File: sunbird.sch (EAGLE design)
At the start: 68 parts, among them J1 USB_MINI-B_SMT, Q8010 600mA/40V, U1000 TP4056, U1500 FS312F-G, U1550 FS8205, U2000 MT3608, U2100 M3406, U4000 FM116B, U5000 CH340G, U6000 RICHTEK-RT3000CGQM, U6001 0.1uF, U6100 HDC1080NOPAD, Y5000 12Mhz

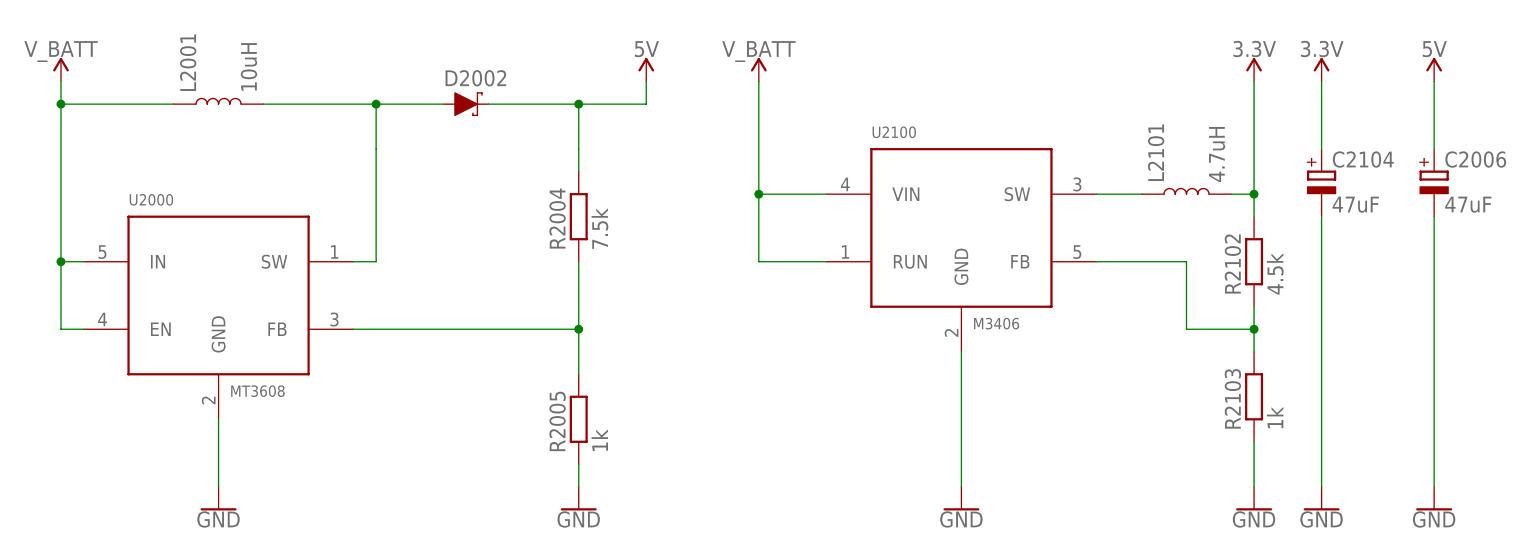
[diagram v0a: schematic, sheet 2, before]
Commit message: Revise PCB to use inductors + 47uF 0603 "miracle" caps from LCSC.
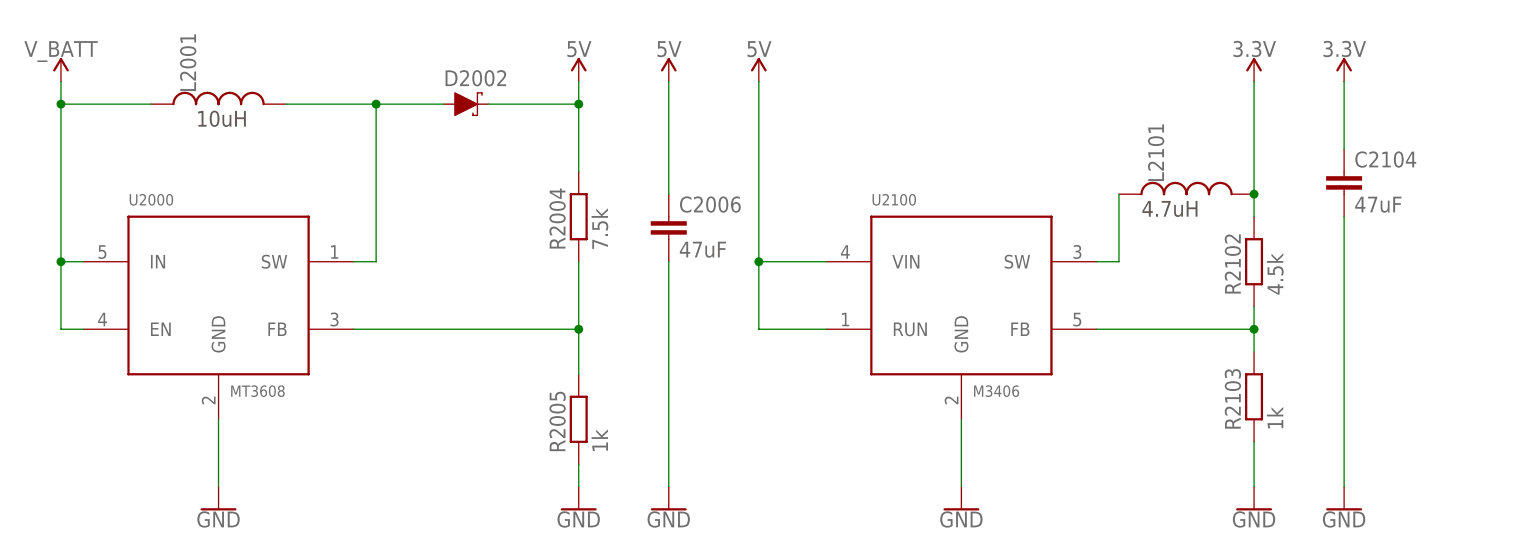
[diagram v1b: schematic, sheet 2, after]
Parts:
- C2006, C2104: device rcl:CPOL-EUUD-5X5,8 -> rcl:C-EUC0603
- L2001, L2101: device SparkFun-Coils:INDUCTOR-0805-3.3UH -> geusebio:INDUCTOR_3.0X3.03.0X3.0
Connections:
- net 3.3V: now also C2104.1; no longer C2104.+
- net 5V: now also C2006.1, U2100.RUN, U2100.VIN; no longer C2006.+
- net GND: now also C2006.2, C2104.2; no longer C2006.-, C2104.-
- net V_BATT: no longer U2100.RUN, U2100.VIN
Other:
- note added: "10uH"
- note added: "4.7uH"
- moved on the sheet: U2100

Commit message: Removing sensor array
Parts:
- removed U6000: RICHTEK-RT3000CGQM, geusebio:RICHTEK-RT3000CGQM
- removed U6001: 0.1uF, rcl:C-EUC0603
- removed U6100: HDC1080NOPAD, geusebio:HDC1080NOPAD
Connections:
- net 3.3V: no longer U6000.VDD, U6000.VDDIO, U6001.1, U6100.VIN
- net ACC_INT/GPIO15: no longer U6000.INT1
- net GND: no longer U6000.GND, U6001.2, U6100.GND
- net SCL/GPIO0: no longer U6000.SCL, U6100.SCL
- net SDA/GPIO4: no longer U6000.SDA, U6100.SDA
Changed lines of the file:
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@@
 <part name="R1009" library="rcl" library_urn="urn:adsk.eagle:library:334" deviceset="R-EU_" device="R0603" package3d_urn="urn:adsk.eagle:package:23555/2" value="2k"/>
 <part name="GND20" library="SparkFun-PowerSymbols" library_urn="urn:adsk.eagle:library:530" deviceset="GND" device=""/>
-<part name="FRAME6" library="SparkFun-Aesthetics" library_urn="urn:adsk.eagle:library:507" deviceset="FRAME-A4L" device=""/>
-<part name="GND21" library="SparkFun-PowerSymbols" library_urn="urn:adsk.eagle:library:530" deviceset="GND" device=""/>
-<part name="SUPPLY23" library="SparkFun-PowerSymbols" library_urn="urn:adsk.eagle:library:530" deviceset="3.3V" device=""/>
-<part name="SUPPLY24" library="SparkFun-PowerSymbols" library_urn="urn:adsk.eagle:library:530" deviceset="3.3V" device=""/>
-<part name="GND22" library="SparkFun-PowerSymbols" library_urn="urn:adsk.eagle:library:530" deviceset="GND" device=""/>
-<part name="U6001" library="rcl" library_urn="urn:adsk.eagle:library:334" deviceset="C-EU" device="C0603" package3d_urn="urn:adsk.eagle:package:23616/2" value="0.1uF"/>
 <part name="R8004" library="rcl" library_urn="urn:adsk.eagle:library:334" deviceset="R-EU_" device="R0603" package3d_urn="urn:adsk.eagle:package:23555/2" value="10k"/>
 <part name="SUPPLY25" library="SparkFun-PowerSymbols" library_urn="urn:adsk.eagle:library:530" deviceset="5V" device=""/>
@@
 <part name="SUPPLY18" library="SparkFun-PowerSymbols" library_urn="urn:adsk.eagle:library:530" deviceset="5V" device=""/>
 <part name="SUPPLY19" library="SparkFun-PowerSymbols" library_urn="urn:adsk.eagle:library:530" deviceset="5V" device=""/>
-<part name="U6000" library="geusebio" deviceset="RICHTEK-RT3000CGQM" device=""/>
 <part name="SUPPLY26" library="SparkFun-PowerSymbols" library_urn="urn:adsk.eagle:library:530" deviceset="5V" device=""/>
-<part name="U6100" library="geusebio" deviceset="HDC1080" device="NOPAD"/>
-<part name="SUPPLY27" library="SparkFun-PowerSymbols" library_urn="urn:adsk.eagle:library:530" deviceset="3.3V" device=""/>
-<part name="GND25" library="SparkFun-PowerSymbols" library_urn="urn:adsk.eagle:library:530" deviceset="GND" device=""/>
 <part name="SUPPLY8" library="SparkFun-PowerSymbols" library_urn="urn:adsk.eagle:library:530" deviceset="5V" device=""/>
 </parts>
@@
 </segment>
 </net>
-</nets>
-</sheet>
-<sheet>
-<description>Sensor Array</description>
-<plain>
-</plain>
-<instances>
-<instance part="FRAME6" gate="G$1" x="0" y="0" smashed="yes">
-<attribute name="DRAWING_NAME" x="181.61" y="11.43" size="2.54" layer="94" font="vector"/>
-<attribute name="LAST_DATE_TIME" x="181.61" y="6.35" size="2.286" layer="94" font="vector"/>
-<attribute name="SHEET" x="195.58" y="1.27" size="2.54" layer="94" font="vector"/>
-</instance>
-<instance part="GND21" gate="1" x="68.58" y="25.4" smashed="yes">
-<attribute name="VALUE" x="68.58" y="25.146" size="1.778" layer="96" align="top-center"/>
-</instance>
-<instance part="SUPPLY23" gate="G$1" x="68.58" y="58.42" smashed="yes">
-<attribute name="VALUE" x="68.58" y="61.214" size="1.778" layer="96" align="bottom-center"/>
-</instance>
-<instance part="SUPPLY24" gate="G$1" x="91.44" y="58.42" smashed="yes">
-<attribute name="VALUE" x="91.44" y="61.214" size="1.778" layer="96" align="bottom-center"/>
-</instance>
-<instance part="GND22" gate="1" x="91.44" y="25.4" smashed="yes">
-<attribute name="VALUE" x="91.44" y="25.146" size="1.778" layer="96" align="top-center"/>
-</instance>
-<instance part="U6001" gate="G$1" x="91.44" y="45.72" smashed="yes">
-<attribute name="NAME" x="92.964" y="46.101" size="1.778" layer="95"/>
-<attribute name="VALUE" x="92.964" y="41.021" size="1.778" layer="96"/>
-</instance>
-<instance part="U6000" gate="G$1" x="55.88" y="40.64" smashed="yes">
-<attribute name="NAME" x="45.72" y="59.69" size="1.27" layer="95"/>
-<attribute name="VALUE" x="45.72" y="27.94" size="1.27" layer="96"/>
-</instance>
-<instance part="U6100" gate="G$1" x="55.88" y="88.9" smashed="yes">
-<attribute name="NAME" x="45.72" y="97.79" size="1.27" layer="95"/>
-<attribute name="VALUE" x="57.15" y="76.2" size="1.27" layer="95"/>
-</instance>
-<instance part="SUPPLY27" gate="G$1" x="55.88" y="104.14" smashed="yes">
-<attribute name="VALUE" x="55.88" y="106.934" size="1.778" layer="96" align="bottom-center"/>
-</instance>
-<instance part="GND25" gate="1" x="55.88" y="68.58" smashed="yes">
-<attribute name="VALUE" x="55.88" y="68.326" size="1.778" layer="96" align="top-center"/>
-</instance>
-</instances>
-<busses>
-</busses>
-<nets>
-<net name="SDA/GPIO4" class="0">
-<segment>
-<wire x1="66.04" y1="45.72" x2="68.58" y2="45.72" width="0.1524" layer="91"/>
-<label x="68.58" y="45.72" size="1.27" layer="95" xref="yes"/>
-<pinref part="U6000" gate="G$1" pin="SDA"/>
-</segment>
-<segment>
-<wire x1="71.12" y1="91.44" x2="73.66" y2="91.44" width="0.1524" layer="91"/>
-<label x="73.66" y="91.44" size="1.27" layer="95" xref="yes"/>
-<pinref part="U6100" gate="G$1" pin="SDA"/>
-</segment>
-</net>
-<net name="SCL/GPIO0" class="0">
-<segment>
-<wire x1="66.04" y1="43.18" x2="68.58" y2="43.18" width="0.1524" layer="91"/>
-<label x="68.58" y="43.18" size="1.27" layer="95" xref="yes"/>
-<pinref part="U6000" gate="G$1" pin="SCL"/>
-</segment>
-<segment>
-<wire x1="71.12" y1="83.82" x2="73.66" y2="83.82" width="0.1524" layer="91"/>
-<label x="73.66" y="83.82" size="1.27" layer="95" xref="yes"/>
-<pinref part="U6100" gate="G$1" pin="SCL"/>
-</segment>
-</net>
-<net name="ACC_INT/GPIO15" class="0">
-<segment>
-<wire x1="66.04" y1="40.64" x2="68.58" y2="40.64" width="0.1524" layer="91"/>
-<label x="68.58" y="40.64" size="1.27" layer="95" xref="yes"/>
-<pinref part="U6000" gate="G$1" pin="INT1"/>
-</segment>
-</net>
-<net name="GND" class="0">
-<segment>
-<wire x1="66.04" y1="33.02" x2="68.58" y2="33.02" width="0.1524" layer="91"/>
-<wire x1="68.58" y1="33.02" x2="68.58" y2="30.48" width="0.1524" layer="91"/>
-<wire x1="68.58" y1="30.48" x2="68.58" y2="27.94" width="0.1524" layer="91"/>
-<pinref part="GND21" gate="1" pin="GND"/>
-<pinref part="U6000" gate="G$1" pin="GND"/>
-</segment>
-<segment>
-<pinref part="GND22" gate="1" pin="GND"/>
-<pinref part="U6001" gate="G$1" pin="2"/>
-<wire x1="91.44" y1="40.64" x2="91.44" y2="27.94" width="0.1524" layer="91"/>
-</segment>
-<segment>
-<pinref part="U6100" gate="G$1" pin="GND"/>
-<pinref part="GND25" gate="1" pin="GND"/>
-<wire x1="55.88" y1="71.12" x2="55.88" y2="73.66" width="0.1524" layer="91"/>
-</segment>
-</net>
-<net name="3.3V" class="0">
-<segment>
-<wire x1="66.04" y1="55.88" x2="68.58" y2="55.88" width="0.1524" layer="91"/>
-<wire x1="66.04" y1="53.34" x2="68.58" y2="53.34" width="0.1524" layer="91"/>
-<wire x1="68.58" y1="53.34" x2="68.58" y2="55.88" width="0.1524" layer="91"/>
-<wire x1="68.58" y1="58.42" x2="68.58" y2="55.88" width="0.1524" layer="91"/>
-<junction x="68.58" y="55.88"/>
-<pinref part="SUPPLY23" gate="G$1" pin="3.3V"/>
-<pinref part="U6000" gate="G$1" pin="VDDIO"/>
-<pinref part="U6000" gate="G$1" pin="VDD"/>
-</segment>
-<segment>
-<pinref part="SUPPLY24" gate="G$1" pin="3.3V"/>
-<pinref part="U6001" gate="G$1" pin="1"/>
-<wire x1="91.44" y1="48.26" x2="91.44" y2="58.42" width="0.1524" layer="91"/>
-</segment>
-<segment>
-<pinref part="U6100" gate="G$1" pin="VIN"/>
-<pinref part="SUPPLY27" gate="G$1" pin="3.3V"/>
-<wire x1="55.88" y1="104.14" x2="55.88" y2="101.6" width="0.1524" layer="91"/>
-</segment>
-</net>

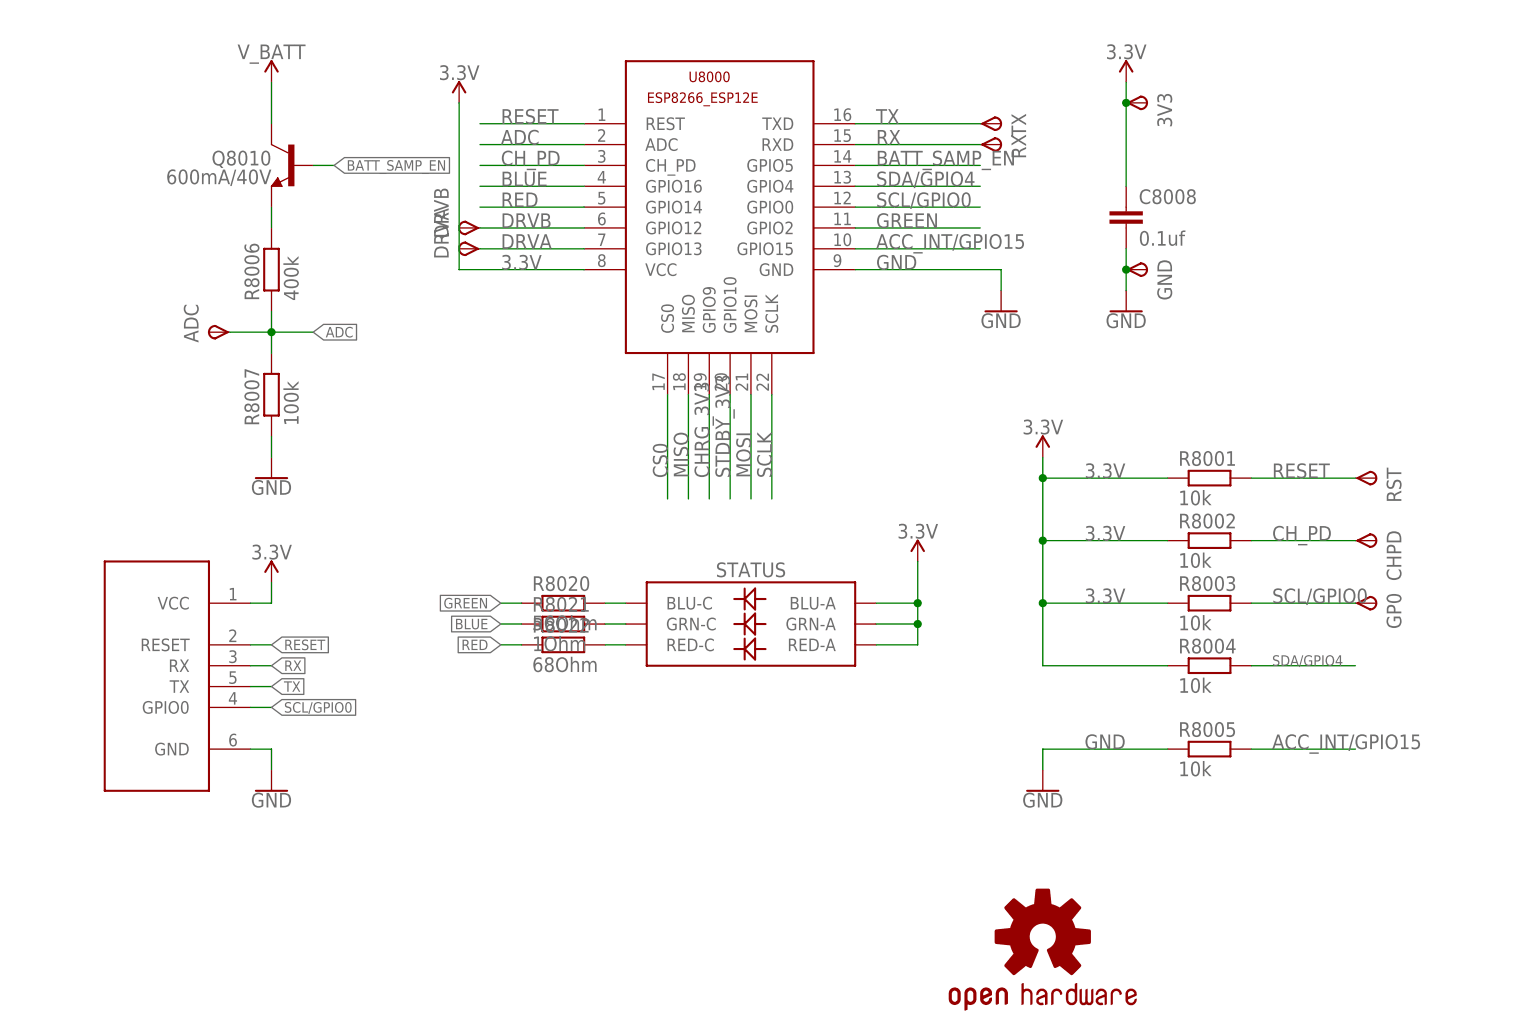
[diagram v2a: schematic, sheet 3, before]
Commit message: Rejig layout, add measurement indexes
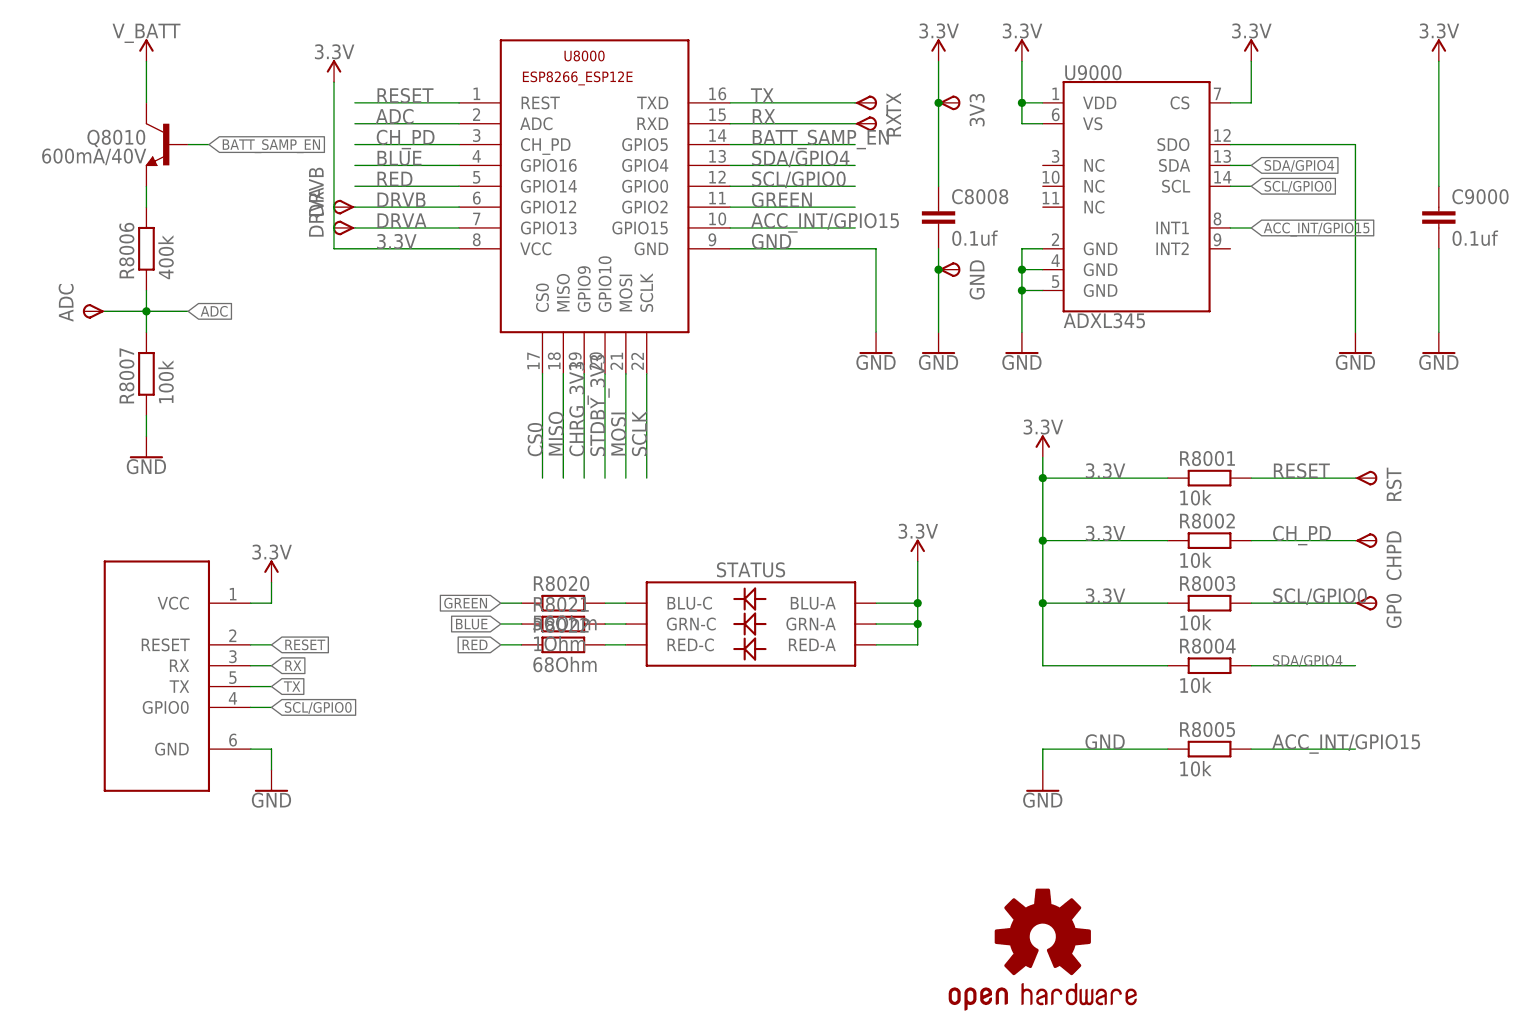
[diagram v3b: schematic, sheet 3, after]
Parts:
- added C9000: 0.1uf, rcl:C-EUC0603
- added U9000: ADXL345, SparkFun-Sensors:ADXL345
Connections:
- net 3.3V: now also C9000.1, U9000.CS, U9000.VDD, U9000.VS
- net ACC_INT/GPIO15: now also U9000.INT1
- net GND: now also C9000.2, U9000.GND@2, U9000.GND@4, U9000.GND@5, U9000.SDO
- net SCL/GPIO0: now also U9000.SCL
- net SDA/GPIO4: now also U9000.SDA
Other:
- moved on the sheet: 3V3, ADC, C8008, DRVA, DRVB, GND, Q8010, R8006, R8007, RX, TX, U8000

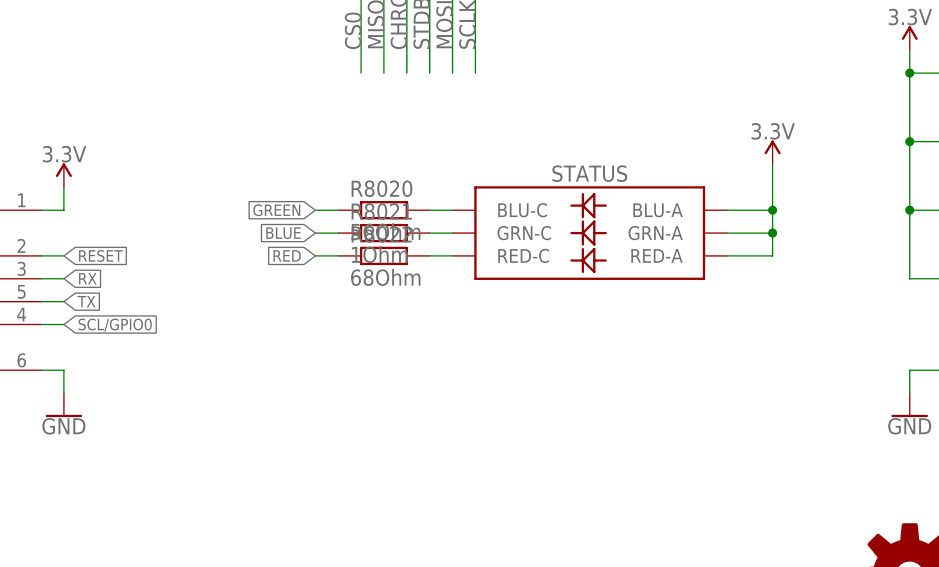
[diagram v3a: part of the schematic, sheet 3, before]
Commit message: Added USB-C socket. Put a copy of the RGB LED on the rear side. Rejigged components.
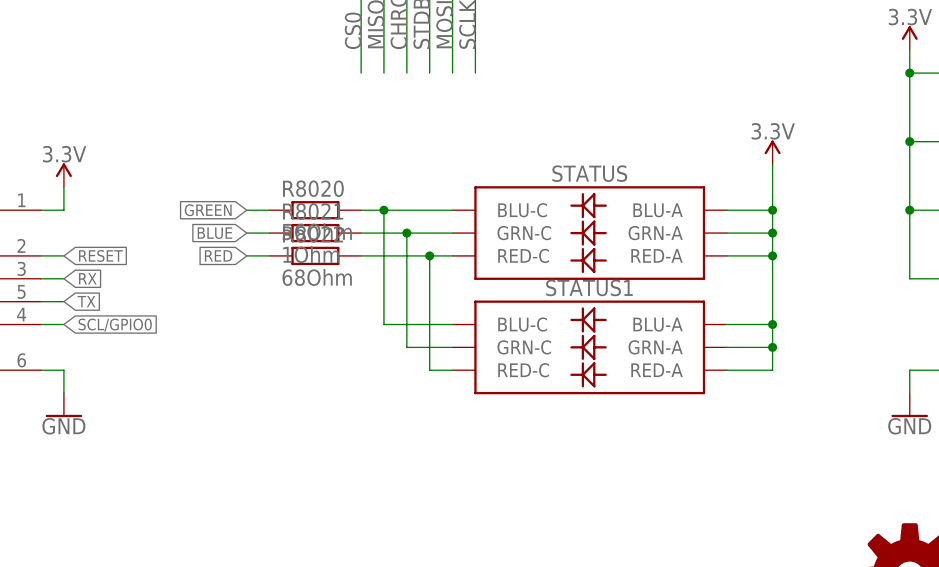
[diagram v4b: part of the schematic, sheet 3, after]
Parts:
- removed J1: USB_MINI-B_SMT, SparkFun-Connectors:USB_MINI-B_SMT
- added STATUS1: (no value), SparkFun-LED:LED-RGBNO_IC
- added U$2: USB-C, geusebio:USB-C
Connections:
- removed net USB_N: J1.D-, U5000.D-
- removed net USB_P: J1.D+, U5000.D+
- new net D+: U$2.D+, U5000.D+
- new net D-: U$2.D-, U5000.D-
- net 3.3V: now also STATUS1.BLU-A, STATUS1.GRN-A, STATUS1.RED-A
- net GND: now also U$2.GND; no longer J1.GND, J1.SHIELD
- net N$14: now also STATUS1.BLU-C
- net N$15: now also STATUS1.GRN-C
- net N$16: now also STATUS1.RED-C
- net V_USB_UNFUSED: now also U$2.VBUS; no longer J1.VBUS
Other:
- moved on the sheet: R8020, R8021, R8022
